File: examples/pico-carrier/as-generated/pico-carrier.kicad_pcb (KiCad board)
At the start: 2 copper layers, 88 x 62 mm, 9 parts, among them J1 5V IN, J3 GP0-GP15, J4 GP16-GP28, PWR, U1 Pico

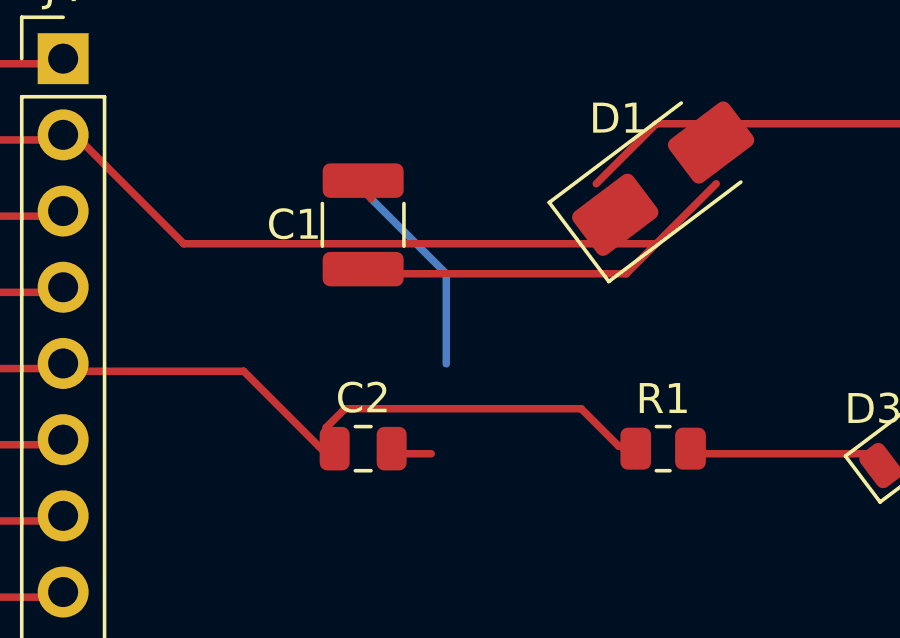
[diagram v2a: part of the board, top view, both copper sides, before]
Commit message: Let a link finish on its own net's copper instead of the pad it names
Every junction on these boards sat on a pad, because a pad was the only
place the router was allowed to stop: a net with three branches funnelled
all three into one 0402, and the reviewer circled the result - converging
diagonals meeting on C15. People do not draw that; they tap the trunk at
the nearest point.

So the search may now end on any cell whose centre lies exactly on the
net's own copper (a tee), with two guards that took one broken board each
to learn: only copper already joined to the link's endpoint counts, or the
named pad is left unconnected; and only a pad-named endpoint may be teed
away from, because a link aimed at a bare coordinate is aimed at the
stated end of a trunk someone drew, and stopping short strands the
trunk's tail. A landing mid-segment is inserted into the trunk's points as
a stated corner, so the reshaping passes pin the join like any other.

The op-amp board shows the effect: 12% less copper, fewer corners, longer
strokes, same connectivity - DRC clean, gates clean, zero crossings on all
four regenerated boards.

Co-Authored-By: Claude Fable 5 <noreply@anthropic.com>
Claude-Session: https://claude.ai/code/session_01DUj7Ltu92tWg159mCSacwY
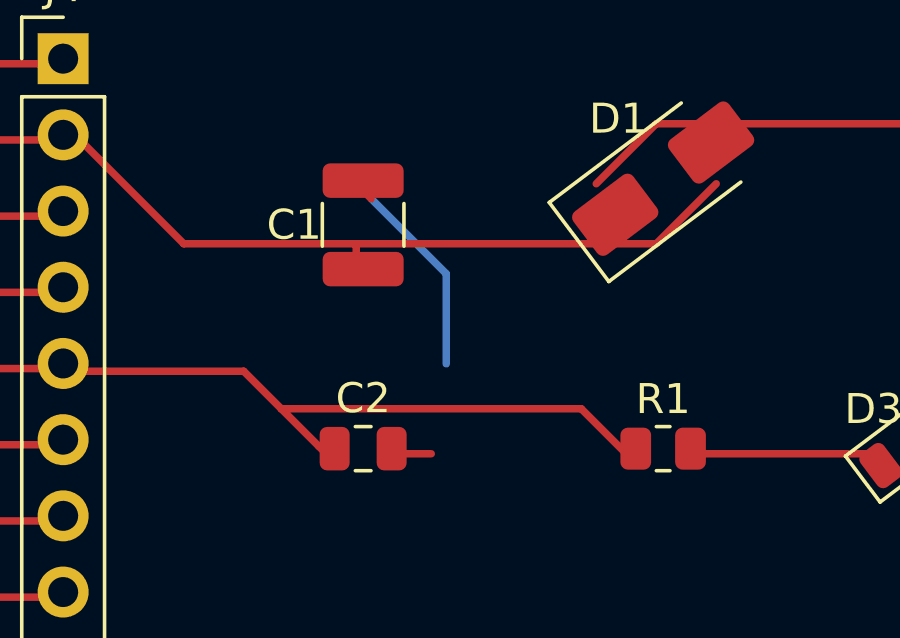
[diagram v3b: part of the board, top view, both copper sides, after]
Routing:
- net /VSYS: track 41.0 -> 31.6 mm
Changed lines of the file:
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@@
 	(segment (start 142.25 66.5) (end 142.75 66.5) (width 0.25) (layer "F.Cu") (net 36))
 	(segment (start 142.75 66.5) (end 146.25 70.0) (width 0.25) (layer "F.Cu") (net 36))
-	(segment (start 146.25 70.0) (end 162.0 70.0) (width 0.25) (layer "F.Cu") (net 36))
+	(segment (start 146.25 70.0) (end 152.0 70.0) (width 0.25) (layer "F.Cu") (net 36))
 	(segment (start 135.69 71.62) (end 135.92 71.62) (width 0.25) (layer "F.Cu") (net 4))
 	(segment (start 135.92 71.62) (end 142.0 71.62) (width 0.25) (layer "F.Cu") (net 4))
@@
 	(segment (start 142.23 74.25) (end 142.25 74.25) (width 0.25) (layer "F.Cu") (net 2))
 	(segment (start 142.25 74.25) (end 148.25 74.25) (width 0.25) (layer "F.Cu") (net 2))
-	(segment (start 148.25 74.25) (end 150.75 76.75) (width 0.25) (layer "F.Cu") (net 2))
-	(segment (start 150.75 76.75) (end 151.0 77.0) (width 0.25) (layer "F.Cu") (net 2))
-	(segment (start 151.0 77.0) (end 151.05 77.0) (width 0.25) (layer "F.Cu") (net 2))
-	(segment (start 151.05 77.0) (end 151.05 76.83) (width 0.25) (layer "F.Cu") (net 2))
-	(segment (start 151.05 76.83) (end 151.05 76.8) (width 0.25) (layer "F.Cu") (net 2))
-	(segment (start 151.05 76.8) (end 151.0 76.75) (width 0.25) (layer "F.Cu") (net 2))
-	(segment (start 151.0 76.75) (end 151.0 76.125) (width 0.25) (layer "F.Cu") (net 2))
-	(segment (start 151.0 76.125) (end 151.625 75.5) (width 0.25) (layer "F.Cu") (net 2))
-	(segment (start 151.625 75.5) (end 159.5 75.5) (width 0.25) (layer "F.Cu") (net 2))
-	(segment (start 159.5 75.5) (end 160.75 76.75) (width 0.25) (layer "F.Cu") (net 2))
-	(segment (start 160.75 76.75) (end 160.8375 76.75) (width 0.25) (layer "F.Cu") (net 2))
-	(segment (start 160.8375 76.75) (end 161.0875 77.0) (width 0.25) (layer "F.Cu") (net 2))
+	(segment (start 148.25 74.25) (end 149.5 75.5) (width 0.25) (layer "F.Cu") (net 2))
 	(segment (start 135.69 76.7) (end 135.92 76.7) (width 0.25) (layer "F.Cu") (net 5))
 	(segment (start 135.92 76.7) (end 142.0 76.7) (width 0.25) (layer "F.Cu") (net 5))
@@
 	(segment (start 163.8273 66.0) (end 162.0 66.0) (width 0.25) (layer "F.Cu") (net 3))
 	(segment (start 162.0 66.0) (end 160.0 68.0) (width 0.25) (layer "F.Cu") (net 3))
-	(segment (start 152.0 71.015) (end 152.23 71.015) (width 0.25) (layer "F.Cu") (net 36))
-	(segment (start 152.23 71.015) (end 152.235 71.015) (width 0.25) (layer "F.Cu") (net 36))
-	(segment (start 152.235 71.015) (end 152.25 71.0) (width 0.25) (layer "F.Cu") (net 36))
-	(segment (start 152.25 71.0) (end 161.0 71.0) (width 0.25) (layer "F.Cu") (net 36))
-	(segment (start 161.0 71.0) (end 164.0 68.0) (width 0.25) (layer "F.Cu") (net 36))
+	(segment (start 164.0 68.0) (end 162.0 70.0) (width 0.25) (layer "F.Cu") (net 36))
+	(segment (start 162.0 70.0) (end 152.0 70.0) (width 0.25) (layer "F.Cu") (net 36))
+	(segment (start 152.0 71.015) (end 152.0 70.845) (width 0.25) (layer "F.Cu") (net 36))
+	(segment (start 152.0 70.845) (end 152.0 70.0) (width 0.25) (layer "F.Cu") (net 36))
+	(segment (start 151.05 77.0) (end 151.0 77.0) (width 0.25) (layer "F.Cu") (net 2))
+	(segment (start 151.0 77.0) (end 150.75 76.75) (width 0.25) (layer "F.Cu") (net 2))
+	(segment (start 150.75 76.75) (end 149.5 75.5) (width 0.25) (layer "F.Cu") (net 2))
+	(segment (start 161.0875 77.0) (end 161.0 77.0) (width 0.25) (layer "F.Cu") (net 2))
+	(segment (start 161.0 77.0) (end 159.5 75.5) (width 0.25) (layer "F.Cu") (net 2))
+	(segment (start 159.5 75.5) (end 149.5 75.5) (width 0.25) (layer "F.Cu") (net 2))
 	(segment (start 162.9125 77.0) (end 163.1425 77.0) (width 0.25) (layer "F.Cu") (net 33))
 	(segment (start 163.1425 77.0) (end 169.0625 77.0) (width 0.25) (layer "F.Cu") (net 33))

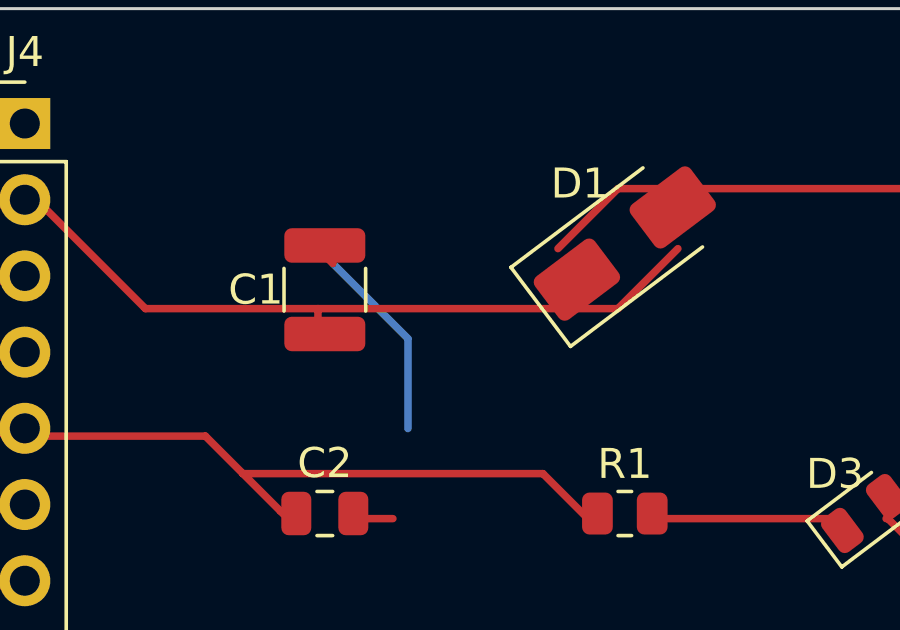
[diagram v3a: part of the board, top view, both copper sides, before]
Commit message: Treat the ground plane as part of the drawing
Six reviewer circles, five of them the plane seen from different corners.
The pour now stops 1.2 mm inside the outline so an edge-hugging trace
keeps shell copper outside it; dead-end tongues narrower than 0.9 mm
retract instead of tapering to an acid-trap point in a bent corner; every
piece of the front pour over 8 mm2 holds a stitching via of its own,
placed before the orphan drop so a fenced-off strip gets a via instead of
staying a blank; and zone clearance comes down from 0.4 to 0.25, which is
what lets the plane flow between a 2.54 mm header's pins instead of
slotting the board top to bottom.

The round-twelve tee learns one manner: within two millimetres of the
goal it stands aside, so a rail flows through a bypass capacitor's pad
instead of feeding it by a stub - the carrier's bulk capacitor also moves
onto the VSYS run it was a millimetre south of. And
readability.margin_intrusion now measures symbol fields, power symbols
included: zero findings across KiCad's 18 demo sheets, one real catch on
our own motor sheet, whose power connector - like the FPGA board's -
moves in from the sheet edge so its printed name clears the frame.

Co-Authored-By: Claude Fable 5 <noreply@anthropic.com>
Claude-Session: https://claude.ai/code/session_01DUj7Ltu92tWg159mCSacwY
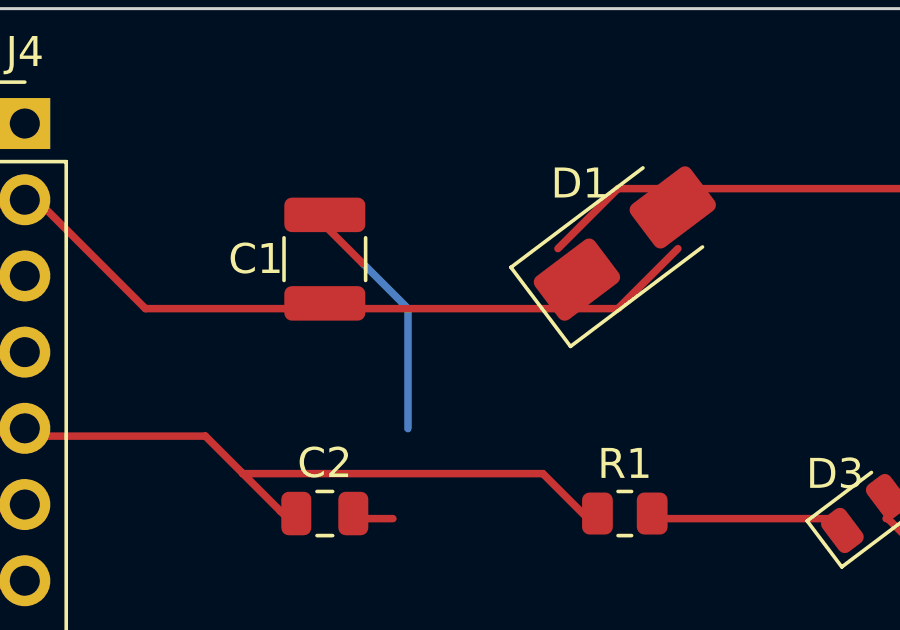
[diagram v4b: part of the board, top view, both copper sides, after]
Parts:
- moved C1 1.02 mm to (152.2, 68.3)
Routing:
- net /VSYS: track 31.6 -> 30.6 mm
- net GND: track 64.7 -> 65.7 mm
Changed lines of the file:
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@@
   )
   (footprint "Capacitor_SMD:C_1210_3225Metric"
-    (at 152.23 69.37 90.0)
+    (at 152.23 68.35 90.0)
     (layer "F.Cu")
     (descr "Capacitor SMD 1210 (3225 Metric), square (rectangular) end terminal, IPC-7351 nominal, (Body size source: IPC-SM-782 page 76, https://www.pcb-3d.com/wordpress/wp-content/uploads/ipc-sm-782a_amendment_1_and_2.pdf), generated with kicad-footprint-generator")
@@
 	(segment (start 135.69 94.48) (end 142.0 94.48) (width 0.25) (layer "F.Cu") (net 1))
 	(segment (start 135.69 107.18) (end 142.0 107.18) (width 0.25) (layer "F.Cu") (net 1))
-	(segment (start 152.0 68.065) (end 152.065 68.065) (width 0.25) (layer "F.Cu") (net 1))
-	(segment (start 152.065 68.065) (end 152.25 68.25) (width 0.25) (layer "F.Cu") (net 1))
-	(segment (start 152.25 68.25) (end 152.5 68.5) (width 0.25) (layer "F.Cu") (net 1))
-	(segment (start 152.5 68.5) (end 155.0 71.0) (width 0.25) (layer "B.Cu") (net 1))
-	(segment (start 155.0 71.0) (end 155.0 74.0) (width 0.25) (layer "B.Cu") (net 1))
+	(segment (start 152.0 67.045) (end 152.045 67.045) (width 0.25) (layer "F.Cu") (net 1))
+	(segment (start 152.045 67.045) (end 152.25 67.25) (width 0.25) (layer "F.Cu") (net 1))
+	(segment (start 152.25 67.25) (end 153.5 68.5) (width 0.25) (layer "F.Cu") (net 1))
+	(segment (start 153.5 68.5) (end 155.0 70.0) (width 0.25) (layer "B.Cu") (net 1))
+	(segment (start 155.0 70.0) (end 155.0 74.0) (width 0.25) (layer "B.Cu") (net 1))
 	(segment (start 152.95 77.0) (end 154.5 77.0) (width 0.25) (layer "F.Cu") (net 1))
 	(segment (start 170.9375 77.0) (end 171.0 77.0) (width 0.25) (layer "F.Cu") (net 1))
@@
 	(segment (start 142.75 66.5) (end 146.25 70.0) (width 0.25) (layer "F.Cu") (net 36))
 	(segment (start 146.25 70.0) (end 152.0 70.0) (width 0.25) (layer "F.Cu") (net 36))
+	(segment (start 152.0 70.0) (end 152.23 70.0) (width 0.25) (layer "F.Cu") (net 36))
+	(segment (start 152.23 70.0) (end 162.0 70.0) (width 0.25) (layer "F.Cu") (net 36))
+	(segment (start 162.0 70.0) (end 164.0 68.0) (width 0.25) (layer "F.Cu") (net 36))
 	(segment (start 135.69 71.62) (end 135.92 71.62) (width 0.25) (layer "F.Cu") (net 4))
 	(segment (start 135.92 71.62) (end 142.0 71.62) (width 0.25) (layer "F.Cu") (net 4))
@@
 	(segment (start 163.8273 66.0) (end 162.0 66.0) (width 0.25) (layer "F.Cu") (net 3))
 	(segment (start 162.0 66.0) (end 160.0 68.0) (width 0.25) (layer "F.Cu") (net 3))
-	(segment (start 164.0 68.0) (end 162.0 70.0) (width 0.25) (layer "F.Cu") (net 36))
-	(segment (start 162.0 70.0) (end 152.0 70.0) (width 0.25) (layer "F.Cu") (net 36))
-	(segment (start 152.0 71.015) (end 152.0 70.845) (width 0.25) (layer "F.Cu") (net 36))
-	(segment (start 152.0 70.845) (end 152.0 70.0) (width 0.25) (layer "F.Cu") (net 36))
 	(segment (start 151.05 77.0) (end 151.0 77.0) (width 0.25) (layer "F.Cu") (net 2))
 	(segment (start 151.0 77.0) (end 150.75 76.75) (width 0.25) (layer "F.Cu") (net 2))

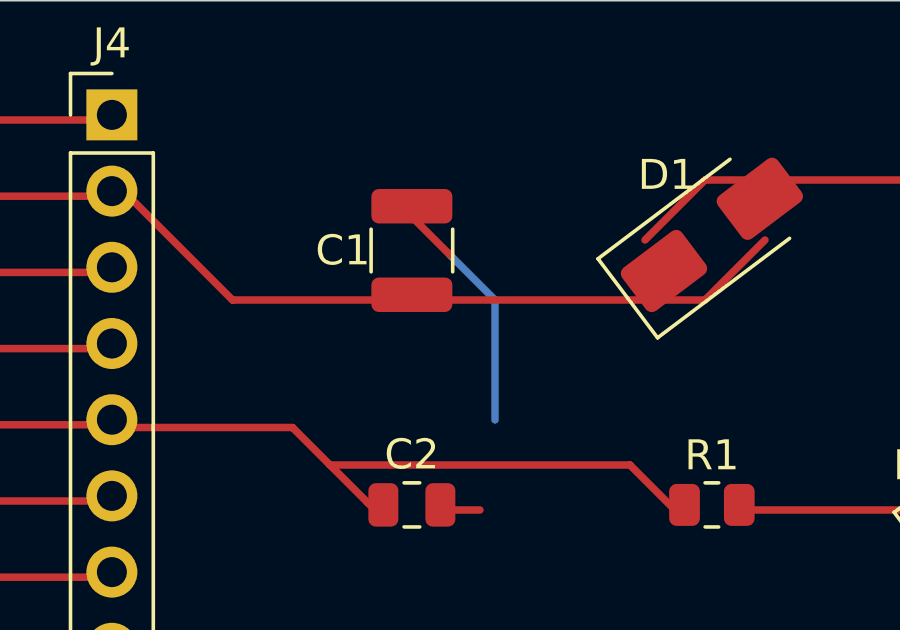
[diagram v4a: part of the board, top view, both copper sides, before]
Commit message: Keep vias out of the lands they would drain
The reviewer's next one, and it is not one board's problem: vias were
landing inside surface-mount lands across the set. A hole in a land is a
hole solder wicks down during reflow - the joint above it starves, and
nothing on the assembled board tells that apart from a cold one.
Via-in-pad is a real technique and a filled-and-capped process, not a
drawing; a layout that has not specified the process may not draw it.

The router was the source. `_blocked` skips a route's own net, so
nothing stopped a layer change from happening on the very land the route
started at, and eighteen vias across three boards sat in one. Pads are
now marked as pads in the obstacle list and every one of them, whoever
owns it, is a cell where a via may not go - so an escape that has to
reach the plane leaves the land first and turns its via beside it. The
stitching pass kept ground vias a via-radius from ground lands where it
kept signal ones a radius plus clearance; both are the same distance
now, because the plane gains nothing from touching a land it can reach a
stub away.

`via.in_pad` measures the copper gap from every via to every land and
reports what is left. The exposed thermal pad under a package is exempt
- the via array in one is the datasheet's own answer, and nothing a
signal reaches is four square millimetres. It blocks under the
ai-generated policy: a generated board has no reason to draw this.

The test fixture had one too, a via twenty-five microns into C1's ground
land; it moves three tenths of a millimetre and the board is DRC clean
on both matrix versions as before.

Co-Authored-By: Claude Fable 5 <noreply@anthropic.com>
Claude-Session: https://claude.ai/code/session_01DUj7Ltu92tWg159mCSacwY
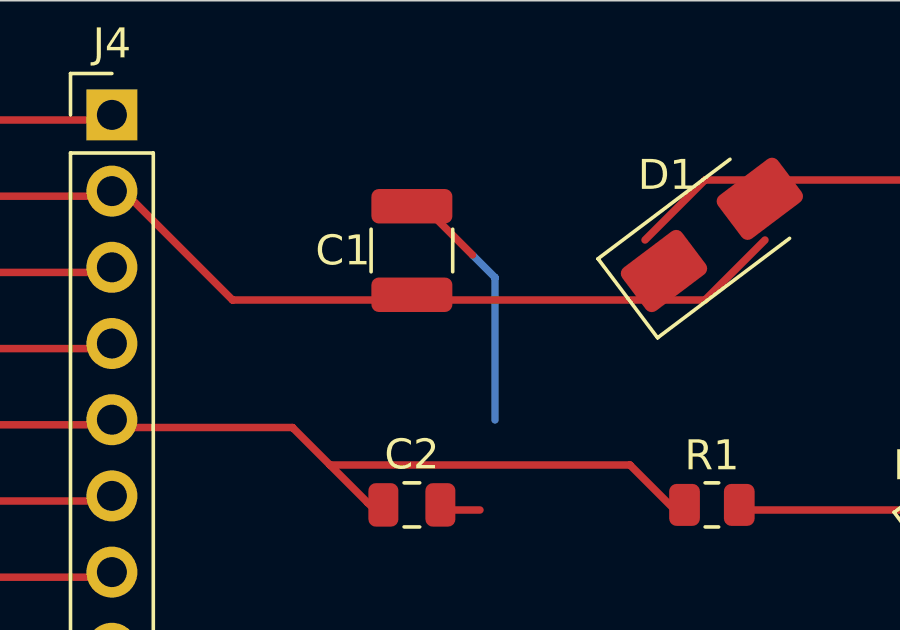
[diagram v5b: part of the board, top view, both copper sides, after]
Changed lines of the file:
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@@
 	(segment (start 135.69 94.48) (end 142.0 94.48) (width 0.25) (layer "F.Cu") (net 1))
 	(segment (start 135.69 107.18) (end 142.0 107.18) (width 0.25) (layer "F.Cu") (net 1))
-	(segment (start 152.0 67.045) (end 152.045 67.045) (width 0.25) (layer "F.Cu") (net 1))
-	(segment (start 152.045 67.045) (end 152.25 67.25) (width 0.25) (layer "F.Cu") (net 1))
-	(segment (start 152.25 67.25) (end 153.5 68.5) (width 0.25) (layer "F.Cu") (net 1))
-	(segment (start 153.5 68.5) (end 155.0 70.0) (width 0.25) (layer "B.Cu") (net 1))
-	(segment (start 155.0 70.0) (end 155.0 74.0) (width 0.25) (layer "B.Cu") (net 1))
+	(segment (start 152.0 67.045) (end 152.205 67.045) (width 0.25) (layer "F.Cu") (net 1))
+	(segment (start 152.205 67.045) (end 152.25 67.0) (width 0.25) (layer "F.Cu") (net 1))
+	(segment (start 152.25 67.0) (end 152.75 67.0) (width 0.25) (layer "F.Cu") (net 1))
+	(segment (start 152.75 67.0) (end 154.25 68.5) (width 0.25) (layer "F.Cu") (net 1))
+	(segment (start 154.25 68.5) (end 155.0 69.25) (width 0.25) (layer "B.Cu") (net 1))
+	(segment (start 155.0 69.25) (end 155.0 74.0) (width 0.25) (layer "B.Cu") (net 1))
 	(segment (start 152.95 77.0) (end 154.5 77.0) (width 0.25) (layer "F.Cu") (net 1))
 	(segment (start 170.9375 77.0) (end 171.0 77.0) (width 0.25) (layer "F.Cu") (net 1))
